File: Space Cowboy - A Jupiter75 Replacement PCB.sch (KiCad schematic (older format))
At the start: 201 parts, among them SW1 SW_PUSH, U1 ATmega32U4-AU, Y1 16MHz

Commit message: Update Space Cowboy - A Jupiter75 Replacement PCB.sch
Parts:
- Y1: LCSC (none) -> C13738
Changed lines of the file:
@@
 F 2 "Crystals:Crystal_SMD_3225-4pin_3.2x2.5mm" H 2900 7300 50  0001 C CNN
 F 3 "~" H 2900 7300 50  0001 C CNN
+F 4 "C13738" V 2900 7300 50  0001 C CNN "LCSC"
 	1    2900 7300
 	0    1    1    0

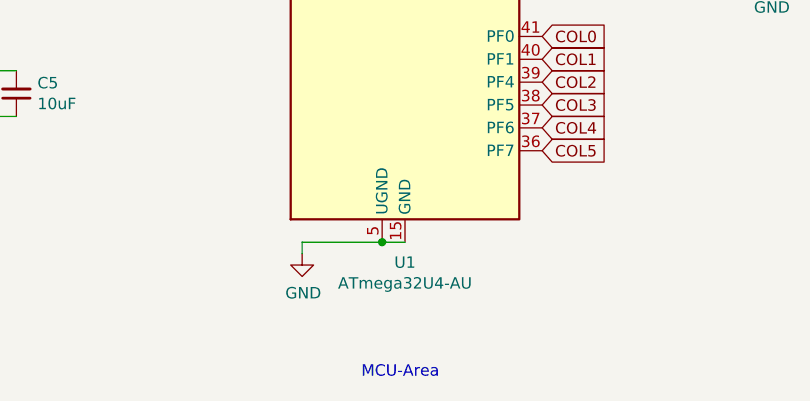
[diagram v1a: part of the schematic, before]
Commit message: Update Space Cowboy - A Jupiter75 Replacement PCB.sch
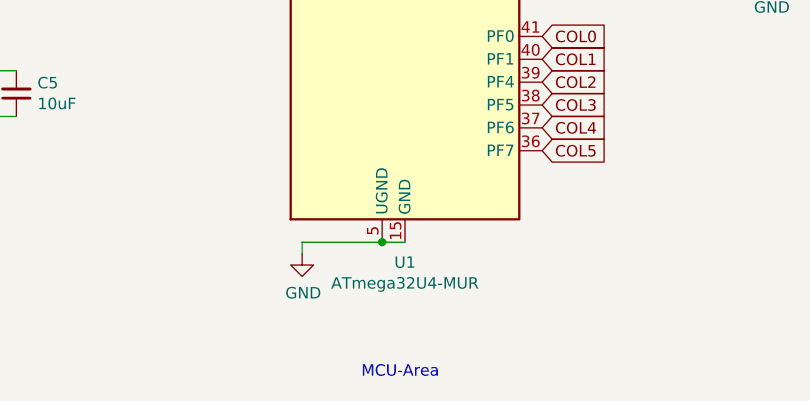
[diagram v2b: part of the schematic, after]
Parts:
- C1: LCSC (none) -> C29936
- C2, C3, C4, C8: LCSC (none) -> C24452
- C5: LCSC (none) -> C96446
- C6, C7: LCSC (none) -> C1653
- D1: LCSC (none) -> C12333
- D10, D11, D12, D13, D14, D15, D16, D17, D18, D19, D2, D20, D21, D22, D23, D24, D25, D26, D27, D28, D29, D3, D30, D31, D32, D33, D34, D35, D36, D37, D38, D39, D4, D40, D41, D42, D43, D44, D45, D46, D47, D48, D49, D5, D50, D51, D52, D53, D54, D55, D56, D57, D58, D59, D6, D60, D61, D62, D63, D64, D65, D66, D67, D68, D69, D7, D70, D71, D72, D73, D74, D75, D76, D77, D78, D79, D8, D80, D81, D82, D83, D84, D85, D9: LCSC (none) -> C81598
- F1: LCSC (none) -> C209741
- R1, R4: LCSC (none) -> C128781
- R5, R6: LCSC (none) -> C146211
- R7: footprint Resistors_SMD:R_0603 -> Resistors_SMD:R_0805; Mfr.Part # (none) -> RN732ATTD5000B25
- SW1: LCSC (none) -> C221856
- U1: value ATmega32U4-AU -> ATmega32U4-MUR; LCSC (none) -> C45874
- USB1: LCSC (none) -> C165948

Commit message: Update Space Cowboy - A Jupiter75 Replacement PCB.sch
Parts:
- R2, R3: LCSC (none) -> C23345
- R5, R6: LCSC C146211 -> C23186
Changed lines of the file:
@@
 F 2 "Resistors_SMD:R_0603" H 2700 8000 50  0001 C CNN
 F 3 "~" H 2700 8000 50  0001 C CNN
+F 4 "C23345" V 2700 8000 50  0001 C CNN "LCSC"
 	1    2700 8000
 	0    -1   -1   0
@@
 F 2 "Resistors_SMD:R_0603" H 2250 8100 50  0001 C CNN
 F 3 "~" H 2250 8100 50  0001 C CNN
+F 4 "C23345" V 2250 8100 50  0001 C CNN "LCSC"
 	1    2250 8100
 	0    1    1    0
@@
 F 2 "Resistors_SMD:R_0603" H 10200 9200 50  0001 C CNN
 F 3 "~" H 10200 9200 50  0001 C CNN
-F 4 "C146211" V 10200 9200 50  0001 C CNN "LCSC"
+F 4 "C23186" V 10200 9200 50  0001 C CNN "LCSC"
 	1    10200 9200
 	0    -1   -1   0
@@
 F 2 "Resistors_SMD:R_0603" H 10200 9800 50  0001 C CNN
 F 3 "~" H 10200 9800 50  0001 C CNN
-F 4 "C146211" V 10200 9800 50  0001 C CNN "LCSC"
+F 4 "C23186" V 10200 9800 50  0001 C CNN "LCSC"
 	1    10200 9800
 	0    -1   -1   0

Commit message: Update Space Cowboy - A Jupiter75 Replacement PCB.sch
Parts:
- R7: LCSC (none) -> C17722; Mfr.Part # RN732ATTD5000B25 -> (none)
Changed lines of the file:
@@
 F 2 "Resistors_SMD:R_0805" H 5100 7700 50  0001 C CNN
 F 3 "~" H 5100 7700 50  0001 C CNN
-F 4 "RN732ATTD5000B25" V 5100 7700 50  0001 C CNN "Mfr.Part #"
+F 4 "C17722" V 5100 7700 50  0001 C CNN "LCSC"
 	1    5100 7700
 	0    1    1    0
